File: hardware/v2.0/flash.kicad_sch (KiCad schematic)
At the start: 10 parts, among them U1 ECP5U-25F-CABGA256, U12 W25Q128JVS

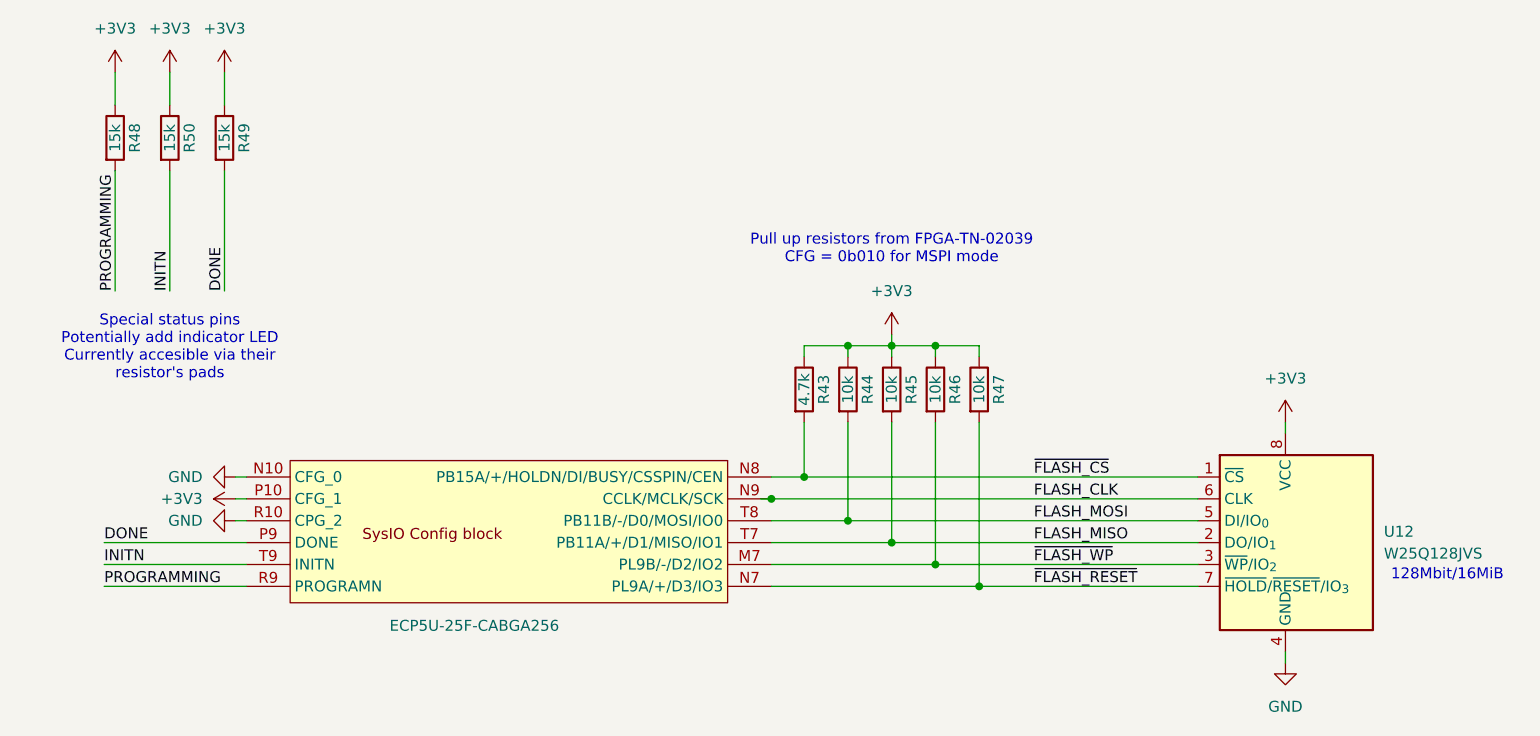
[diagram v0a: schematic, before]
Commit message: ADC 6 diff lines
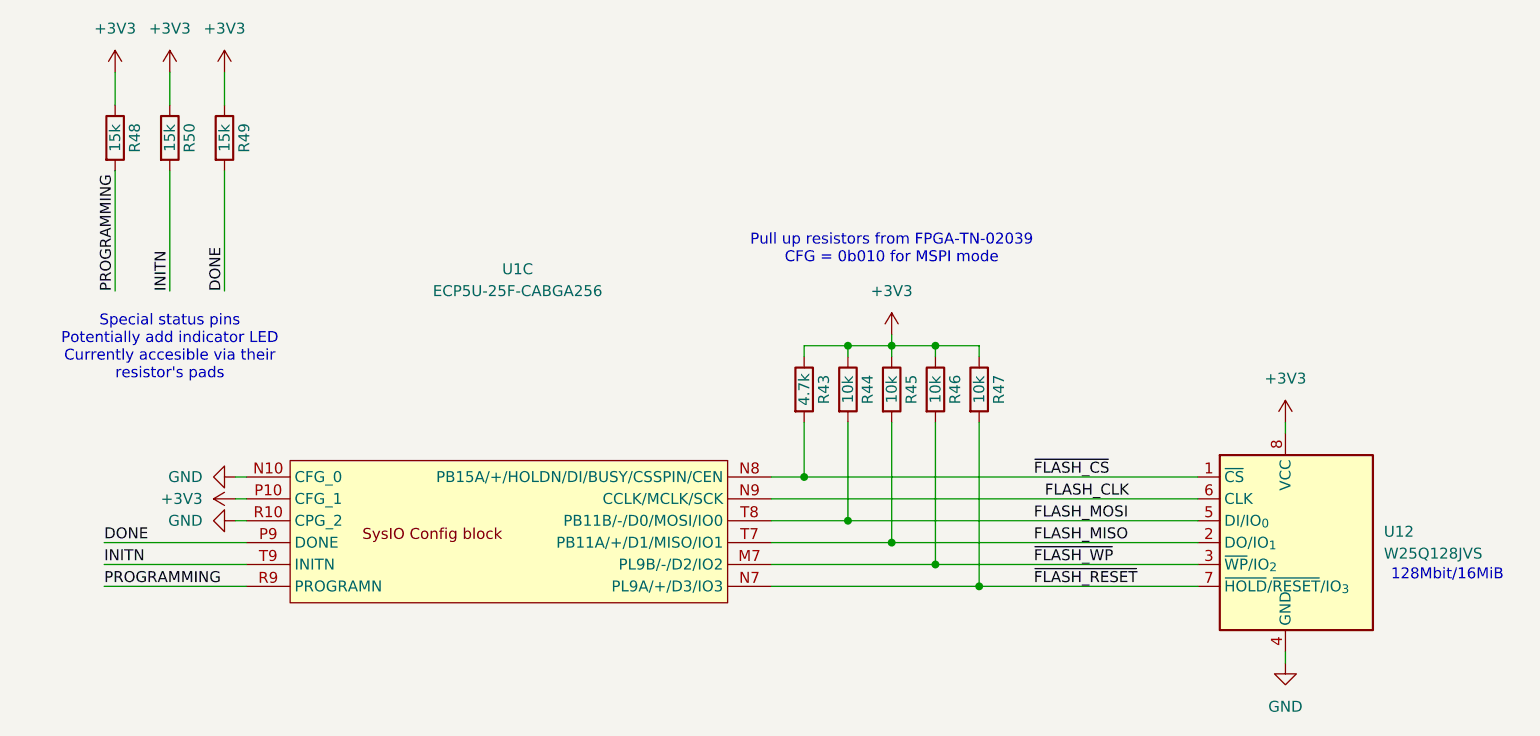
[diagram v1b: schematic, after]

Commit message: ADC CLKOUT±
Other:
- company: Chengyin Yao (cheyao), Vadym Vikulin -> Vadym Vikulin, Chengyin Yao (cheyao)
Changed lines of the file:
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@@
 	(title_block
 		(title "Icepi Zero")
-		(date "2026-01-05")
-		(rev "v2.0")
-		(company "Chengyin Yao (cheyao), Vadym Vikulin")
-		(comment 1 "https://github.com/cheyao/icepi-zero")
+		(date "2026-01-17")
+		(rev "v2.1")
+		(company "Vadym Vikulin, Chengyin Yao (cheyao)")
+		(comment 1 "https://github.com/vikulin/icepi-zero")
 		(comment 2 "License: Solderpad")
 		(comment 9 "OSHWA FR000026")
@@
 		(pin "F8"
 		)
+		(pin "N6"
+		)
 		(instances

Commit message: BOM fields unification for PCBWay requirements
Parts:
- R43: MANUFACTURER (none) -> UNI-ROYAL; MANUFACTURER_PART_NUMBER (none) -> 0402WGF4701TCE
- R44, R45, R46, R47: MANUFACTURER (none) -> UNI-ROYAL; MANUFACTURER_PART_NUMBER (none) -> 0402WGF1002TCE
- R48, R49, R50: MANUFACTURER (none) -> UNI-ROYAL; MANUFACTURER_PART_NUMBER (none) -> 0402WGF1502TCE
- U1: MANUFACTURER (none) -> Lattice; MANUFACTURER_PART_NUMBER (none) -> LFE5U-25F-6BG256C
- U12: MANUFACTURER (none) -> Winbond; MANUFACTURER_PART_NUMBER (none) -> W25Q128JVSIQ
